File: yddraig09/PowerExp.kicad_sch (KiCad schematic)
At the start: 24 parts, among them J10 Expansion, J11 PwrLED, J12 57PC5F, SW3 PowerSwitch, U44 TC1262-3.3VAB

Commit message: Updated yddraig09 silkscreen
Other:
- title: Y Ddraig Fechan -> Y Ddraig Fach
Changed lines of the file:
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@@
   (paper "A4")
   (title_block
-    (title "Y Ddraig Fechan")
+    (title "Y Ddraig Fach")
     (company "Stephen Moody")
   )

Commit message: Small updates to 6809 and 030 board, remove old files
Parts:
- renumbered C88 to C49, C89 to C50, C90 to C51, C91 to C52, C92 to C53, C93 to C54, C94 to C55, C95 to C56, C96 to C57, C97 to C58, D6 to D5, D7 to D6, D8 to D7, J10 to J11, J11 to J12, J12 to J13, R45 to R28, R46 to R29, R47 to R30, R48 to R31, U44 to U28

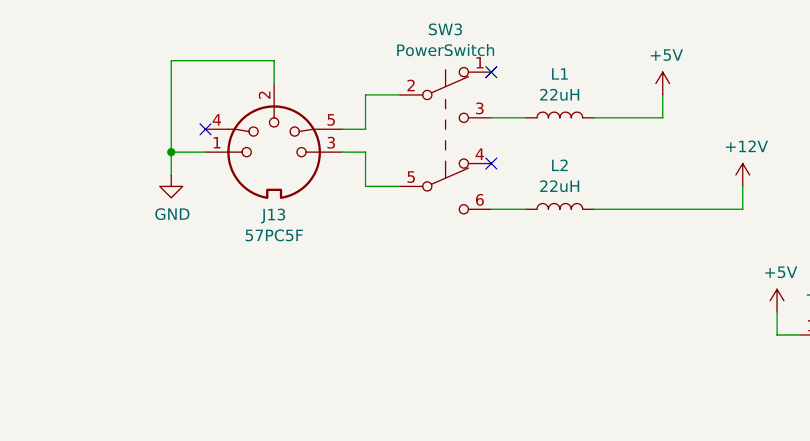
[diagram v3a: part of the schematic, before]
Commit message: All projects updated to KiCAD 7 format files
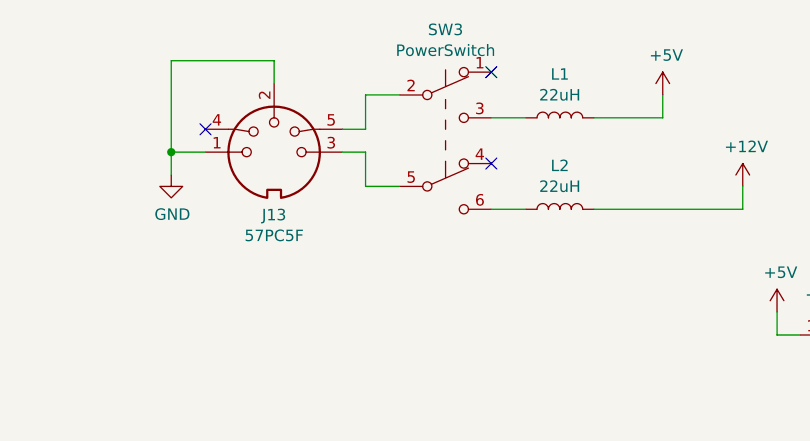
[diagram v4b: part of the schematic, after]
